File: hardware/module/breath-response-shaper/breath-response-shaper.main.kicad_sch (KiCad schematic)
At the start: 10 parts

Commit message: WIP module schematics: footprints, bought-part fields, and the two board projects (module-main, module-jack)
Recovered from a container restart; not yet exported or checked.

Co-Authored-By: Claude Opus 5.5 <noreply@anthropic.com>
Claude-Session: https://claude.ai/code/session_01LmB4muFXnoLprWX4JzuJ5A
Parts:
- C-DEC-RESP-NEG, C-DEC-RESP-POS: footprint (none) -> Capacitor_SMD:C_0805_2012Metric; Assembly (none) -> machine; LCSC (none) -> C49678; MPN (none) -> CC0805KRX7R9BB104; Manufacturer (none) -> YAGEO
- D-RESP-A, D-RESP-B: footprint (none) -> Diode_SMD:D_SOD-123; Assembly (none) -> machine; LCSC (none) -> C241939; MPN (none) -> 1N4148W-E3-08; Manufacturer (none) -> Vishay
- R-RESP: footprint (none) -> Resistor_SMD:R_0805_2012Metric; Assembly (none) -> machine; LCSC (none) -> C17475; MPN (none) -> 0805W8F1502T5E; Manufacturer (none) -> UNI-ROYAL(Uniroyal Elec)
- R-RESP-DIV-HI, R-RESP-DIV-LO, R-RESP-FB: footprint (none) -> Resistor_SMD:R_0805_2012Metric; Assembly (none) -> machine; LCSC (none) -> C17414; MPN (none) -> 0805W8F1002T5E; Manufacturer (none) -> UNI-ROYAL(Uniroyal Elec)
- R-RESP-IN: footprint (none) -> Resistor_SMD:R_0805_2012Metric; Assembly (none) -> machine; LCSC (none) -> C4328; MPN (none) -> 0805W8F2002T5E; Manufacturer (none) -> UNI-ROYAL(Uniroyal Elec)
- U-RESP: footprint (none) -> Package_SO:SOIC-8_3.9x4.9mm_P1.27mm; Assembly (none) -> machine; LCSC (none) -> C139363; MPN (none) -> OPA2197IDR; Manufacturer (none) -> Texas Instruments

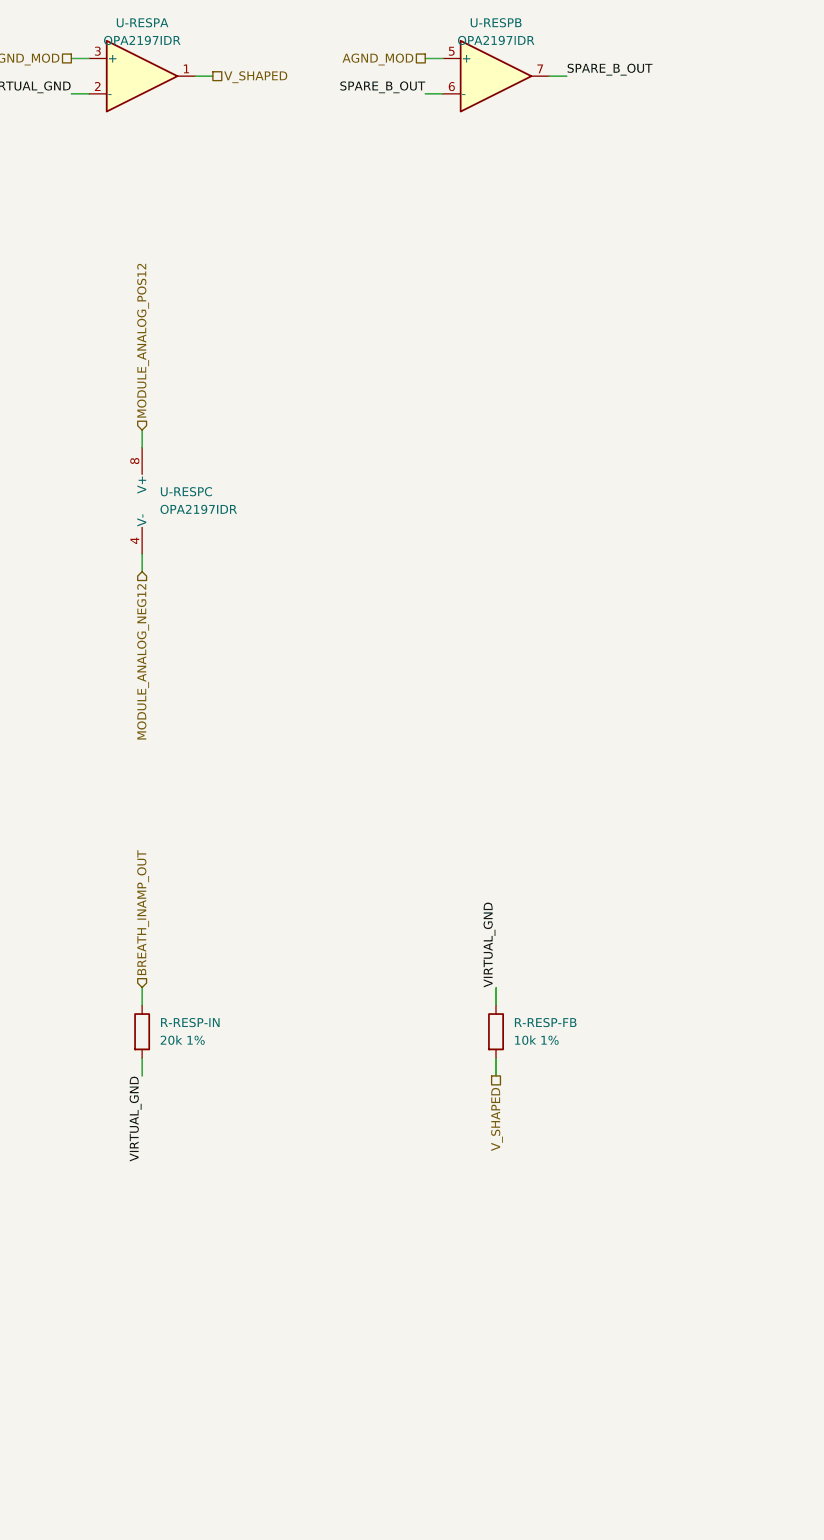
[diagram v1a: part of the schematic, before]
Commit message: Breath response shaper adopted: restoring half drawn, output feeds POT-GAIN; pots ordered to fit the knob
U-RESP B restores x2 inverting (R-RESTORE-IN 10k, R-RESTORE-FB 20k): unity and
the in-amp's polarity at centre detent. BREATH_SHAPED feeds POT-GAIN on
J-B2B-MOD pin 1; nets.yaml moves the shaper from proposed to fitted.
POT-GAIN linear (the design's working gain sits at noon); POT-OFFSET gets no
detent. POT-GAIN/OFFSET are Song Huei R0904N KC (18-tooth, the T18 knob's
shaft; KQ is 40-tooth); POT-RESP Alpha RV09AF-40-25B-B50K-0C (18-tooth B shaft,
centre click). POT-OFFSET's zero is +18.7 deg on the 280-deg track, not 300.

Co-Authored-By: Claude Opus 5.5 <noreply@anthropic.com>
Claude-Session: https://claude.ai/code/session_01LmB4muFXnoLprWX4JzuJ5A
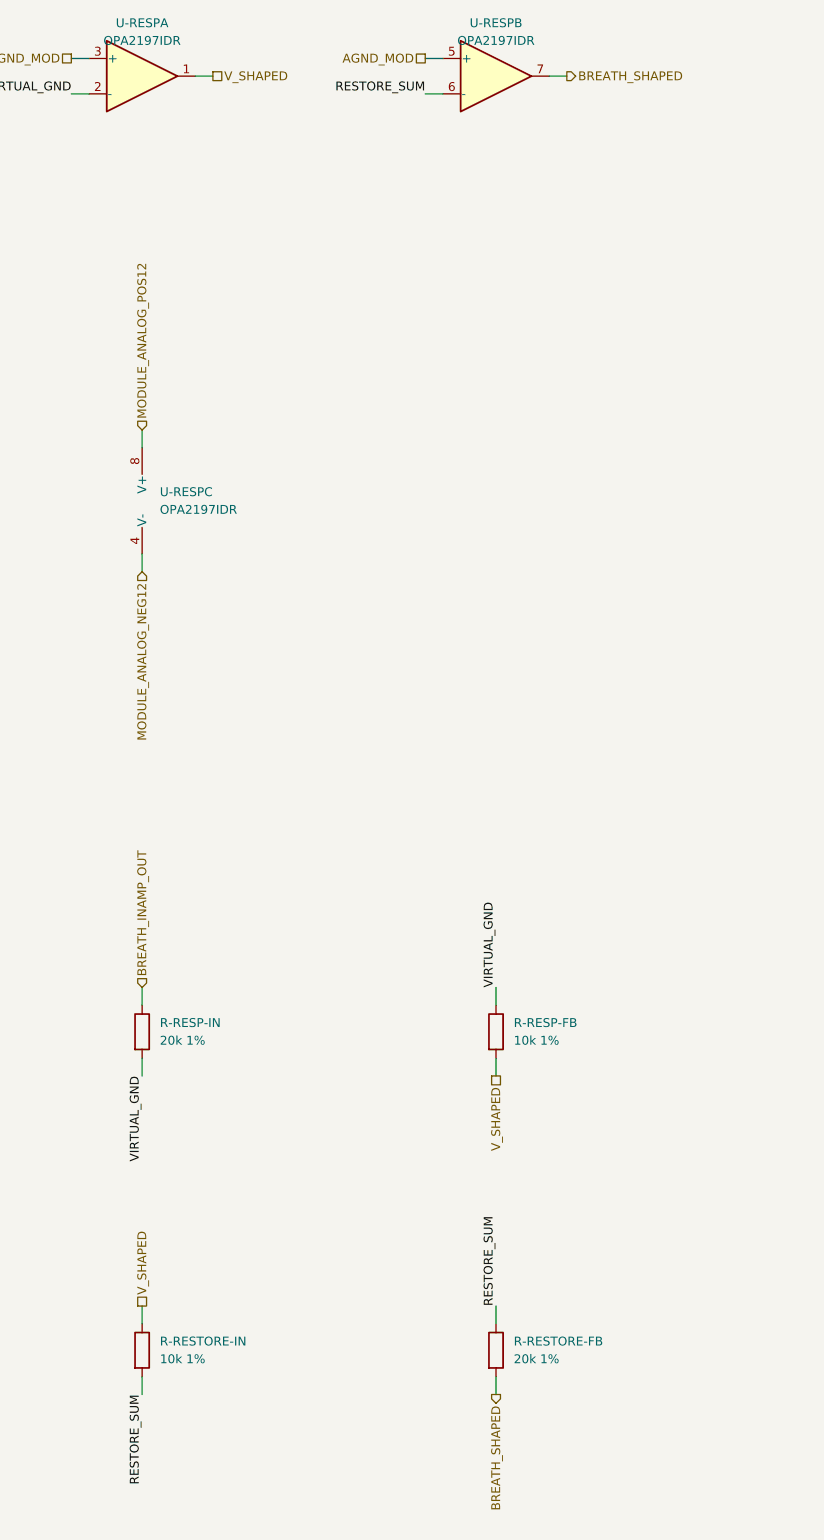
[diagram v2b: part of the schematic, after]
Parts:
- added R-RESTORE-FB: 20k 1%, Resistor_SMD:R_0805_2012Metric, symbol Device:R
- added R-RESTORE-IN: 10k 1%, Resistor_SMD:R_0805_2012Metric, symbol Device:R
- U-RESP: Note Half A is the shaping half, inverting at /2. Half B is the restoring x2 half, which is not drawn: tied off as a follower until it is -> Half A is the shaping half, inverting at /2. Half B is the restoring half, inverting at x2 (R-RESTORE-IN, R-RESTORE-FB), whose output BREATH_SHAPED feeds POT-GAIN
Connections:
- net V_SHAPED: now also R-RESTORE-IN.1
- net SPARE_B_OUT renamed BREATH_SHAPED
- net BREATH_SHAPED: now also R-RESTORE-FB.2; no longer U-RESP.6 (-)
- new net RESTORE_SUM: R-RESTORE-FB.1, R-RESTORE-IN.2, U-RESP.6 (-)
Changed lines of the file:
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@@
     (property "Row" "U-RESP" (at 40.64 50.8 0) (effects (font (size 1.27 1.27)) hide))
     (property "Pins" "INA+=3(+) INA-=2(-) OUTA=1(~) INB+=5(+) INB-=6(-) OUTB=7(~) V+=8(V+) V-=4(V-)" (at 40.64 50.8 0) (effects (font (size 1.27 1.27)) hide))
-    (property "Note" "Half A is the shaping half, inverting at /2. Half B is the restoring x2 half, which is not drawn: tied off as a follower until it is" (at 40.64 50.8 0) (effects (font (size 1.27 1.27)) hide))
+    (property "Note" "Half A is the shaping half, inverting at /2. Half B is the restoring half, inverting at x2 (R-RESTORE-IN, R-RESTORE-FB), whose output BREATH_SHAPED feeds POT-GAIN" (at 40.64 50.8 0) (effects (font (size 1.27 1.27)) hide))
     (property "Pins_source" "datasheets/analog/OPA2197.pdf section 5, D package (SOIC-8), OPA2197: OUT A 1, -IN A 2, +IN A 3, V- 4, +IN B 5, -IN B 6, OUT B 7, V+ 8" (at 40.64 50.8 0) (effects (font (size 1.27 1.27)) hide))
     (property "Manufacturer" "Texas Instruments" (at 40.64 50.8 0) (effects (font (size 1.27 1.27)) hide))
@@
     (property "Row" "U-RESP" (at 91.44 50.8 0) (effects (font (size 1.27 1.27)) hide))
     (property "Pins" "INA+=3(+) INA-=2(-) OUTA=1(~) INB+=5(+) INB-=6(-) OUTB=7(~) V+=8(V+) V-=4(V-)" (at 91.44 50.8 0) (effects (font (size 1.27 1.27)) hide))
-    (property "Note" "Half A is the shaping half, inverting at /2. Half B is the restoring x2 half, which is not drawn: tied off as a follower until it is" (at 91.44 50.8 0) (effects (font (size 1.27 1.27)) hide))
+    (property "Note" "Half A is the shaping half, inverting at /2. Half B is the restoring half, inverting at x2 (R-RESTORE-IN, R-RESTORE-FB), whose output BREATH_SHAPED feeds POT-GAIN" (at 91.44 50.8 0) (effects (font (size 1.27 1.27)) hide))
     (property "Pins_source" "datasheets/analog/OPA2197.pdf section 5, D package (SOIC-8), OPA2197: OUT A 1, -IN A 2, +IN A 3, V- 4, +IN B 5, -IN B 6, OUT B 7, V+ 8" (at 91.44 50.8 0) (effects (font (size 1.27 1.27)) hide))
     (property "Manufacturer" "Texas Instruments" (at 91.44 50.8 0) (effects (font (size 1.27 1.27)) hide))
@@
     (property "Row" "U-RESP" (at 40.64 111.75999999999999 0) (effects (font (size 1.27 1.27)) hide))
     (property "Pins" "INA+=3(+) INA-=2(-) OUTA=1(~) INB+=5(+) INB-=6(-) OUTB=7(~) V+=8(V+) V-=4(V-)" (at 40.64 111.75999999999999 0) (effects (font (size 1.27 1.27)) hide))
-    (property "Note" "Half A is the shaping half, inverting at /2. Half B is the restoring x2 half, which is not drawn: tied off as a follower until it is" (at 40.64 111.75999999999999 0) (effects (font (size 1.27 1.27)) hide))
+    (property "Note" "Half A is the shaping half, inverting at /2. Half B is the restoring half, inverting at x2 (R-RESTORE-IN, R-RESTORE-FB), whose output BREATH_SHAPED feeds POT-GAIN" (at 40.64 111.75999999999999 0) (effects (font (size 1.27 1.27)) hide))
     (property "Pins_source" "datasheets/analog/OPA2197.pdf section 5, D package (SOIC-8), OPA2197: OUT A 1, -IN A 2, +IN A 3, V- 4, +IN B 5, -IN B 6, OUT B 7, V+ 8" (at 40.64 111.75999999999999 0) (effects (font (size 1.27 1.27)) hide))
     (property "Manufacturer" "Texas Instruments" (at 40.64 111.75999999999999 0) (effects (font (size 1.27 1.27)) hide))
@@
     (property "From" "module/power-entry" (at 294.64 181.61 0) (effects (font (size 1.27 1.27)) hide)))
   (wire (pts (xy 99.06 50.8) (xy 101.6 50.8)) (stroke (width 0) (type default)))
-  (label "SPARE_B_OUT" (at 101.6 50.8 0) (fields_autoplaced) (effects (font (size 1.27 1.27)) (justify left bottom)))
+  (hierarchical_label "BREATH_SHAPED" (shape output) (at 101.6 50.8 0) (effects (font (size 1.27 1.27)) (justify left))
+    (property "Dir" "out" (at 101.6 50.8 0) (effects (font (size 1.27 1.27)) hide))
+    (property "To" "module/breath-output-stage" (at 101.6 50.8 0) (effects (font (size 1.27 1.27)) hide)))
   (wire (pts (xy 83.82 53.34) (xy 81.28 53.34)) (stroke (width 0) (type default)))
-  (label "SPARE_B_OUT" (at 81.28 53.34 180) (fields_autoplaced) (effects (font (size 1.27 1.27)) (justify right bottom)))
+  (label "RESTORE_SUM" (at 81.28 53.34 180) (fields_autoplaced) (effects (font (size 1.27 1.27)) (justify right bottom)))
   (wire (pts (xy 48.26 50.8) (xy 50.8 50.8)) (stroke (width 0) (type default)))
   (hierarchical_label "V_SHAPED" (shape passive) (at 50.8 50.8 0) (effects (font (size 1.27 1.27)) (justify left))
@@
   (hierarchical_label "V_SHAPED" (shape passive) (at 91.44 194.31 270) (effects (font (size 1.27 1.27)) (justify right))
     (property "Dir" "ref" (at 91.44 194.31 0) (effects (font (size 1.27 1.27)) hide)))
+  (symbol (lib_id "Device:R") (at 40.64 233.68 0) (unit 1)
+    (in_bom yes) (on_board yes) (dnp no)
+    (property "Reference" "R-RESTORE-IN" (at 43.18 232.41 0) (effects (font (size 1.27 1.27)) (justify left)))
+    (property "Value" "10k 1%" (at 43.18 234.95 0) (effects (font (size 1.27 1.27)) (justify left)))
+    (property "Footprint" "Resistor_SMD:R_0805_2012Metric" (at 40.64 233.68 0) (effects (font (size 1.27 1.27)) hide))
+    (property "Datasheet" "" (at 40.64 233.68 0) (effects (font (size 1.27 1.27)) hide))
+    (property "Row" "R-RESTORE-IN" (at 40.64 233.68 0) (effects (font (size 1.27 1.27)) hide))
+    (property "Pins" "1=1 2=2" (at 40.64 233.68 0) (effects (font (size 1.27 1.27)) hide))
+    (property "Note" "Input resistor of the restoring half: V_shaped into U-RESP B's (-) input. With R-RESTORE-FB, x2 inverting" (at 40.64 233.68 0) (effects (font (size 1.27 1.27)) hide))
+    (property "Manufacturer" "UNI-ROYAL(Uniroyal Elec)" (at 40.64 233.68 0) (effects (font (size 1.27 1.27)) hide))
+    (property "MPN" "0805W8F1002T5E" (at 40.64 233.68 0) (effects (font (size 1.27 1.27)) hide))
+    (property "LCSC" "C17414" (at 40.64 233.68 0) (effects (font (size 1.27 1.27)) hide))
+    (property "Assembly" "machine" (at 40.64 233.68 0) (effects (font (size 1.27 1.27)) hide))
+    (pin "1")
+    (pin "2")
+    (instances (project "module-main" (path "/fc77e9f9-9171-5c83-92ae-8cafe880764e/c482d433-655e-5e81-83d2-2324ffc55f2a" (reference "R59") (unit 1))) (project "breath-response-shaper.main" (path "/b720220a-6b4f-50eb-8ff6-c33665ae6827" (reference "R-RESTORE-IN") (unit 1))) (project "breath-response-shaper" (path "/97139bb3-9c58-5159-a2a9-3813e79c635b/c16928c3-e665-533e-bb80-5b6da545f796" (reference "R-RESTORE-IN") (unit 1))))
+  )
+  (wire (pts (xy 40.64 229.87) (xy 40.64 227.33)) (stroke (width 0) (type default)))
+  (hierarchical_label "V_SHAPED" (shape passive) (at 40.64 227.33 90) (effects (font (size 1.27 1.27)) (justify left)))
+  (wire (pts (xy 40.64 237.49) (xy 40.64 240.03)) (stroke (width 0) (type default)))
+  (label "RESTORE_SUM" (at 40.64 240.03 270) (fields_autoplaced) (effects (font (size 1.27 1.27)) (justify right bottom)))
+  (symbol (lib_id "Device:R") (at 91.44 233.68 0) (unit 1)
+    (in_bom yes) (on_board yes) (dnp no)
+    (property "Reference" "R-RESTORE-FB" (at 93.98 232.41 0) (effects (font (size 1.27 1.27)) (justify left)))
+    (property "Value" "20k 1%" (at 93.98 234.95 0) (effects (font (size 1.27 1.27)) (justify left)))
+    (property "Footprint" "Resistor_SMD:R_0805_2012Metric" (at 91.44 233.68 0) (effects (font (size 1.27 1.27)) hide))
+    (property "Datasheet" "" (at 91.44 233.68 0) (effects (font (size 1.27 1.27)) hide))
+    (property "Row" "R-RESTORE-FB" (at 91.44 233.68 0) (effects (font (size 1.27 1.27)) hide))
+    (property "Pins" "1=1 2=2" (at 91.44 233.68 0) (effects (font (size 1.27 1.27)) hide))
+    (property "Note" "Feedback resistor of the restoring half. -20k/10k = -2 undoes the shaping half's -1/2, so at centre detent the stage is exactly unity and polarity is the in-amp's" (at 91.44 233.68 0) (effects (font (size 1.27 1.27)) hide))
+    (property "Manufacturer" "UNI-ROYAL(Uniroyal Elec)" (at 91.44 233.68 0) (effects (font (size 1.27 1.27)) hide))
+    (property "MPN" "0805W8F2002T5E" (at 91.44 233.68 0) (effects (font (size 1.27 1.27)) hide))
+    (property "LCSC" "C4328" (at 91.44 233.68 0) (effects (font (size 1.27 1.27)) hide))
+    (property "Assembly" "machine" (at 91.44 233.68 0) (effects (font (size 1.27 1.27)) hide))
+    (pin "1")
+    (pin "2")
+    (instances (project "module-main" (path "/fc77e9f9-9171-5c83-92ae-8cafe880764e/c482d433-655e-5e81-83d2-2324ffc55f2a" (reference "R60") (unit 1))) (project "breath-response-shaper.main" (path "/b720220a-6b4f-50eb-8ff6-c33665ae6827" (reference "R-RESTORE-FB") (unit 1))) (project "breath-response-shaper" (path "/97139bb3-9c58-5159-a2a9-3813e79c635b/c16928c3-e665-533e-bb80-5b6da545f796" (reference "R-RESTORE-FB") (unit 1))))
+  )
+  (wire (pts (xy 91.44 229.87) (xy 91.44 227.33)) (stroke (width 0) (type default)))
+  (label "RESTORE_SUM" (at 91.44 227.33 90) (fields_autoplaced) (effects (font (size 1.27 1.27)) (justify left bottom)))
+  (wire (pts (xy 91.44 237.49) (xy 91.44 240.03)) (stroke (width 0) (type default)))
+  (hierarchical_label "BREATH_SHAPED" (shape output) (at 91.44 240.03 270) (effects (font (size 1.27 1.27)) (justify right))
+    (property "Dir" "out" (at 91.44 240.03 0) (effects (font (size 1.27 1.27)) hide))
+    (property "To" "module/breath-output-stage" (at 91.44 240.03 0) (effects (font (size 1.27 1.27)) hide)))
   (sheet_instances (path "/" (page "1")))
 )

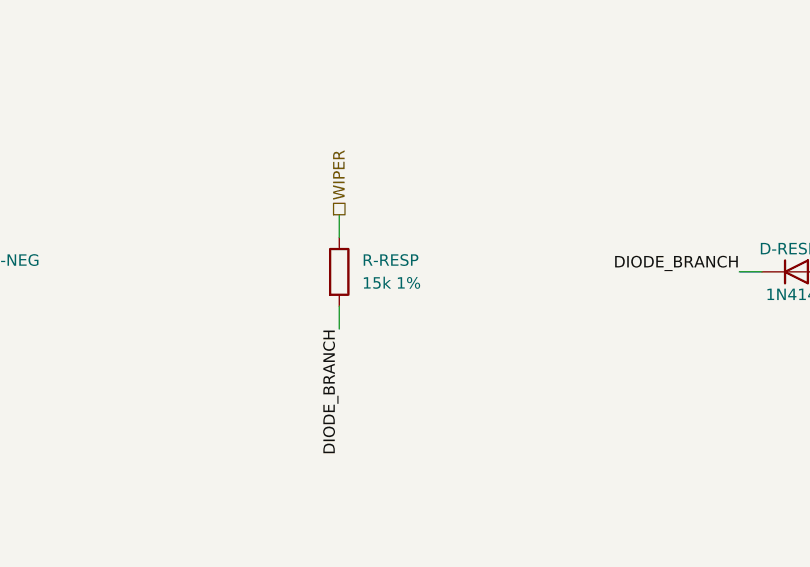
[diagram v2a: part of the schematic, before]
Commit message: Response shaper: R-RESP 3.9k for at least 1.5x at a hard blow at every corner (owner); sim asserts it
Co-Authored-By: Claude Opus 5.5 <noreply@anthropic.com>
Claude-Session: https://claude.ai/code/session_01LmB4muFXnoLprWX4JzuJ5A
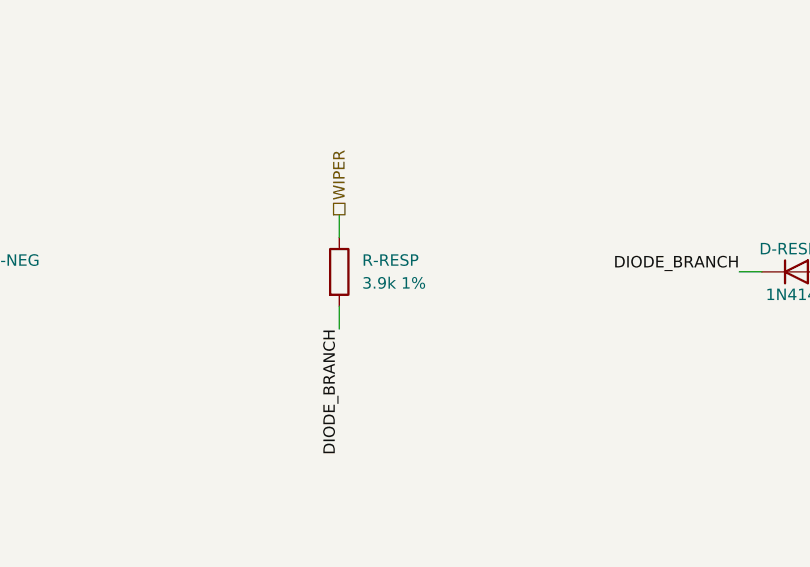
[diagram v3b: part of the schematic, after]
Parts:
- R-RESP: value 15k 1% -> 3.9k 1%; LCSC C17475 -> C17614; MPN 0805W8F1502T5E -> 0805W8F3901T5E; Note Sets how hard the curve bends. 15k is a FIRST SIZING for ab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 -> Sets how hard the curve bends: shaper-exp-gain, at least 1.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
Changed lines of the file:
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@@
     (in_bom yes) (on_board yes) (dnp no)
     (property "Reference" "R-RESP" (at 347.98 186.69 0) (effects (font (size 1.27 1.27)) (justify left)))
-    (property "Value" "15k 1%" (at 347.98 189.23 0) (effects (font (size 1.27 1.27)) (justify left)))
+    (property "Value" "3.9k 1%" (at 347.98 189.23 0) (effects (font (size 1.27 1.27)) (justify left)))
     (property "Footprint" "Resistor_SMD:R_0805_2012Metric" (at 344.17 187.96 0) (effects (font (size 1.27 1.27)) hide))
     (property "Datasheet" "" (at 345.44 187.96 0) (effects (font (size 1.27 1.27)) hide))
     (property "Row" "R-RESP" (at 345.44 187.96 0) (effects (font (size 1.27 1.27)) hide))
     (property "Pins" "1=1 2=2" (at 345.44 187.96 0) (effects (font (size 1.27 1.27)) hide))
-    (property "Note" "Sets how hard the curve bends. 15k is a FIRST SIZING for about 1.5x at a hard blow and wants a bench pass with a player" (at 345.44 187.96 0) (effects (font (size 1.27 1.27)) hide))
+    (property "Note" "Sets how hard the curve bends: shaper-exp-gain, at least 1.5x at a hard blow at POT-RESP's CW end at every simulated corner (owner, 2026-09-30: 1.5x). module/breath-response-shaper/sim" (at 345.44 187.96 0) (effects (font (size 1.27 1.27)) hide))
     (property "Manufacturer" "UNI-ROYAL(Uniroyal Elec)" (at 345.44 187.96 0) (effects (font (size 1.27 1.27)) hide))
-    (property "MPN" "0805W8F1502T5E" (at 345.44 187.96 0) (effects (font (size 1.27 1.27)) hide))
-    (property "LCSC" "C17475" (at 345.44 187.96 0) (effects (font (size 1.27 1.27)) hide))
+    (property "MPN" "0805W8F3901T5E" (at 345.44 187.96 0) (effects (font (size 1.27 1.27)) hide))
+    (property "LCSC" "C17614" (at 345.44 187.96 0) (effects (font (size 1.27 1.27)) hide))
     (property "Assembly" "machine" (at 345.44 187.96 0) (effects (font (size 1.27 1.27)) hide))
     (pin "1")
